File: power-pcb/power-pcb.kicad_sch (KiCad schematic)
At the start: 5 parts

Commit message: power-pcb: re-annotate schematic and start board
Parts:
- SYM1: footprint Symbol:ESD-Logo_13.2x12mm_SilkScreen -> Symbol:ESD-Logo_8.9x8mm_SilkScreen
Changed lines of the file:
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@@
 			)
 		)
-		(property "Footprint" "Symbol:ESD-Logo_13.2x12mm_SilkScreen"
+		(property "Footprint" "Symbol:ESD-Logo_8.9x8mm_SilkScreen"
 			(at 21.463 19.812 0)
 			(hide yes)

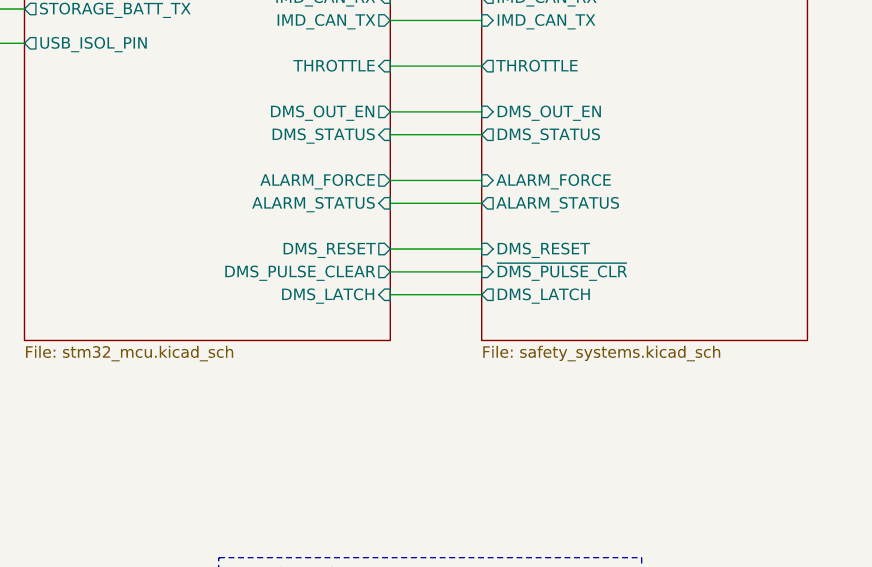
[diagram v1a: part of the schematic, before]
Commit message: power-pcb: fix schematic after review
- Add footprint for resitive load for the RECOM
- Add Opamps when useful
- Add capacitor and change some footprint sizes
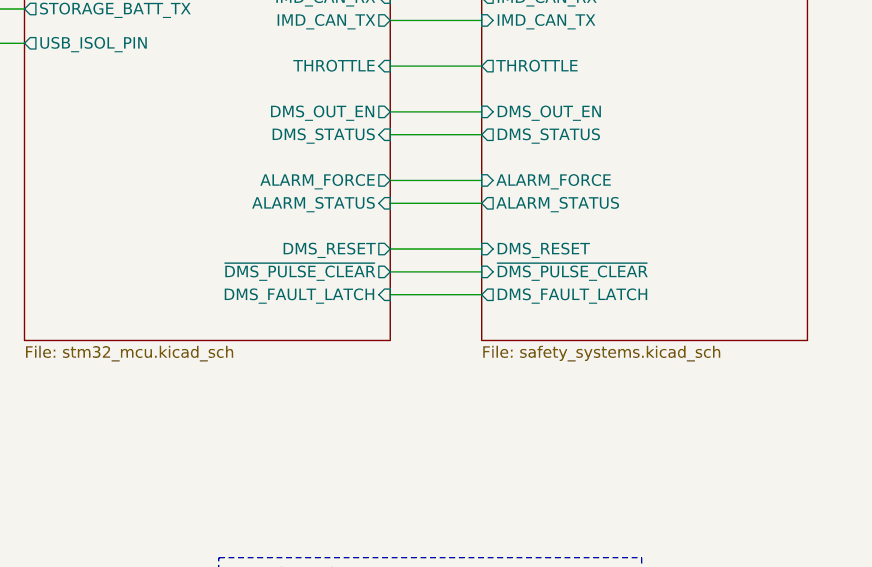
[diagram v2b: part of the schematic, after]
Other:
- sheet STM32 Microcontroller ports: added DMS_FAULT_LATCH, ~{DMS_PULSE_CLEAR}; removed DMS_LATCH, DMS_PULSE_CLEAR
- sheet Safety Systems ports: added DMS_FAULT_LATCH, ~{DMS_PULSE_CLEAR}; removed DMS_LATCH, ~{DMS_PULSE_CLR}
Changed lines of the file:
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@@
+			)
+		)
+		(property "Sim.Library" ""
+			(at 21.59 19.05 0)
+			(hide yes)
+			(show_name no)
+			(do_not_autoplace no)
+			(effects
+				(font
+					(size 1.27 1.27)
+				)
+			)
+		)
+		(property "Sim.Name" ""
+			(at 21.59 19.05 0)
+			(hide yes)
+			(show_name no)
+			(do_not_autoplace no)
+			(effects
+				(font
+					(size 1.27 1.27)
+				)
 			)
 		)
@@
 			)
 		)
+		(property "Sim.Library" ""
+			(at 138.43 182.88 0)
+			(hide yes)
+			(show_name no)
+			(do_not_autoplace no)
+			(effects
+				(font
+					(size 1.27 1.27)
+				)
+			)
+		)
+		(property "Sim.Name" ""
+			(at 138.43 182.88 0)
+			(hide yes)
+			(show_name no)
+			(do_not_autoplace no)
+			(effects
+				(font
+					(size 1.27 1.27)
+				)
+			)
+		)
 		(pin "1"
 		)
@@
 			)
 		)
+		(property "Sim.Library" ""
+			(at 147.32 182.88 0)
+			(hide yes)
+			(show_name no)
+			(do_not_autoplace no)
+			(effects
+				(font
+					(size 1.27 1.27)
+				)
+			)
+		)
+		(property "Sim.Name" ""
+			(at 147.32 182.88 0)
+			(hide yes)
+			(show_name no)
+			(do_not_autoplace no)
+			(effects
+				(font
+					(size 1.27 1.27)
+				)
+			)
+		)
 		(pin "1"
 		)
@@
 		)
 		(property "Description" "Mounting Hole with connection"
+			(at 165.1 182.88 0)
+			(hide yes)
+			(show_name no)
+			(do_not_autoplace no)
+			(effects
+				(font
+					(size 1.27 1.27)
+				)
+			)
+		)
+		(property "Sim.Library" ""
+			(at 165.1 182.88 0)
+			(hide yes)
+			(show_name no)
+			(do_not_autoplace no)
+			(effects
+				(font
+					(size 1.27 1.27)
+				)
+			)
+		)
+		(property "Sim.Name" ""
 			(at 165.1 182.88 0)
 			(hide yes)
@@
 			)
 		)
+		(property "Sim.Library" ""
+			(at 156.21 182.88 0)
+			(hide yes)
+			(show_name no)
+			(do_not_autoplace no)
+			(effects
+				(font
+					(size 1.27 1.27)
+				)
+			)
+		)
+		(property "Sim.Name" ""
+			(at 156.21 182.88 0)
+			(hide yes)
+			(show_name no)
+			(do_not_autoplace no)
+			(effects
+				(font
+					(size 1.27 1.27)
+				)
+			)
+		)
 		(pin "1"
 		)
@@
 			)
 		)
+		(pin "DMS_OUT_EN" input
+			(at 157.48 118.11 180)
+			(effects
+				(font
+					(size 1.27 1.27)
+				)
+				(justify left)
+			)
+		)
+		(pin "DMS_RESET" input
+			(at 157.48 133.35 180)
+			(effects
+				(font
+					(size 1.27 1.27)
+				)
+				(justify left)
+			)
+		)
+		(pin "~{DMS_PULSE_CLEAR}" input
+			(at 157.48 135.89 180)
+			(effects
+				(font
+					(size 1.27 1.27)
+				)
+				(justify left)
+			)
+		)
 		(pin "IMD_CAN_TX" input
 			(at 157.48 107.95 180)
@@
 			)
 		)
-		(pin "DMS_OUT_EN" input
-			(at 157.48 118.11 180)
-			(effects
-				(font
-					(size 1.27 1.27)
-				)
-				(justify left)
-			)
-		)
-		(pin "DMS_LATCH" output
+		(pin "DMS_FAULT_LATCH" output
 			(at 157.48 138.43 180)
-			(effects
-				(font
-					(size 1.27 1.27)
-				)
-				(justify left)
-			)
-		)
-		(pin "DMS_RESET" input
-			(at 157.48 133.35 180)
-			(effects
-				(font
-					(size 1.27 1.27)
-				)
-				(justify left)
-			)
-		)
-		(pin "~{DMS_PULSE_CLR}" input
-			(at 157.48 135.89 180)
 			(effects
 				(font
@@
 			)
 		)
-		(pin "DMS_LATCH" input
-			(at 147.32 138.43 0)
-			(effects
-				(font
-					(size 1.27 1.27)
-				)
-				(justify right)
-			)
-		)
 		(pin "DMS_RESET" output
 			(at 147.32 133.35 0)
@@
 			)
 		)
-		(pin "DMS_PULSE_CLEAR" output
+		(pin "~{DMS_PULSE_CLEAR}" output
 			(at 147.32 135.89 0)
 			(effects
 				(font
+					(size 1.27 1.27)
+				)
+				(justify right)
+			)
+		)
+		(pin "DMS_FAULT_LATCH" input
+			(at 147.32 138.43 0)
+			(effects
+				(font
